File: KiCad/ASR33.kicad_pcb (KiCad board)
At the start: 2 copper layers, 45 x 38 mm, 42 parts, among them J1 USB-C, J2 DC, J3 Power, J4 RUN, J5 Tx, J6 Rx, Q1 NX7002AK, SW1 SW_Push, U1 ESP32-WROOM-32, U2 FT231XQ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

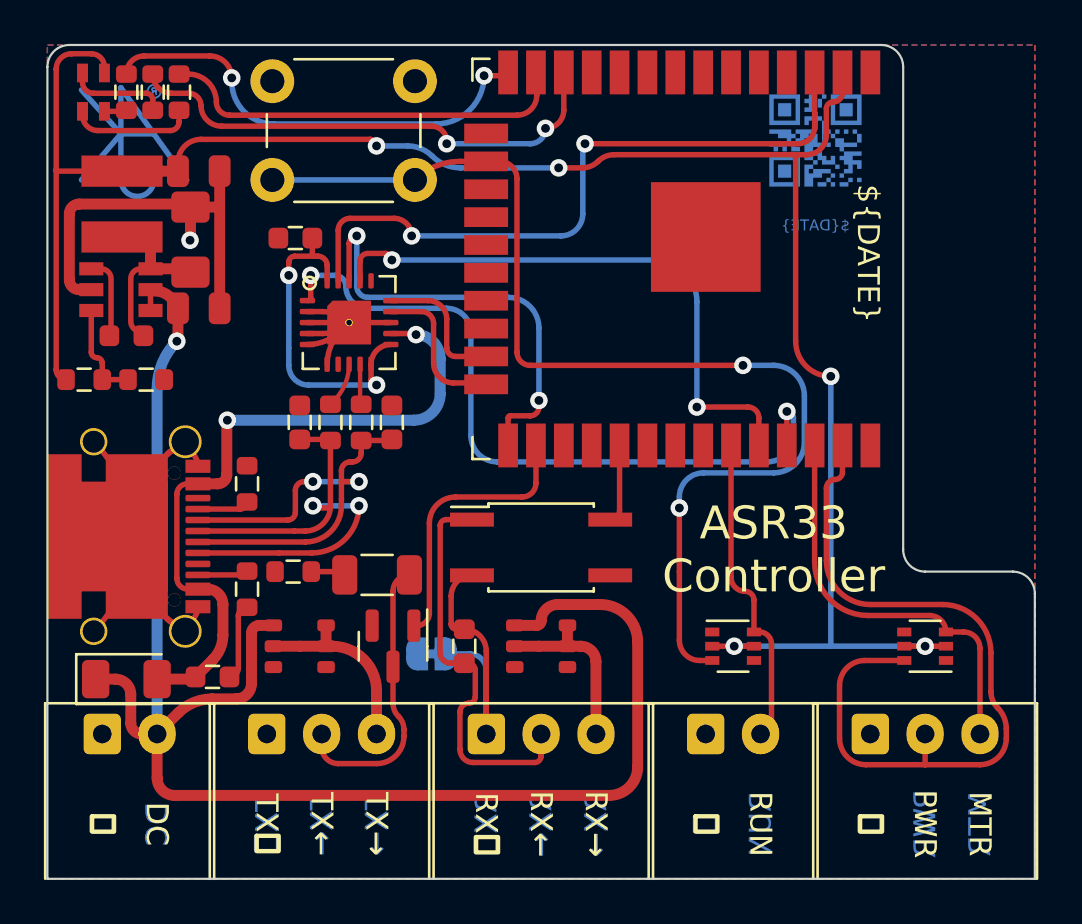
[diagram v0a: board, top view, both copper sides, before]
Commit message: Label GPIOs on silkscreen
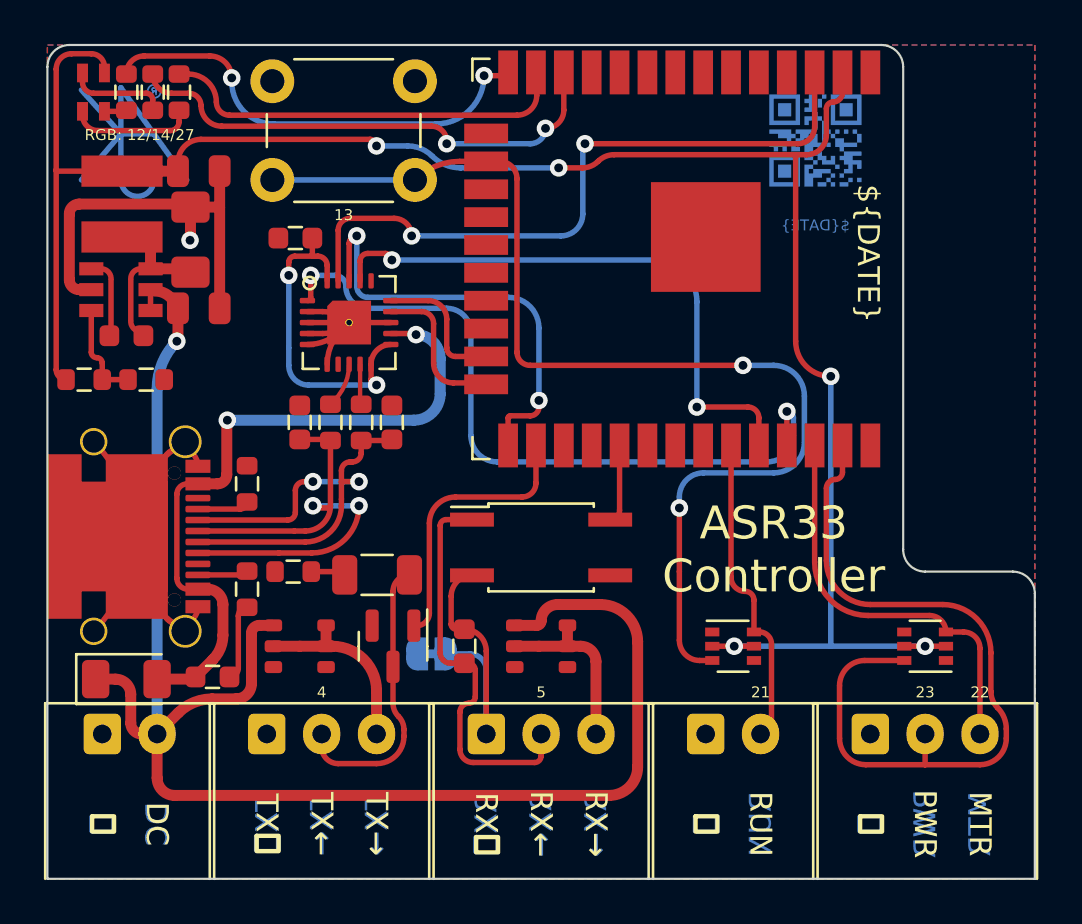
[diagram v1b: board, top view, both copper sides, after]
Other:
- board text added: "13"
- board text added: "21"
- board text added: "22"
- board text added: "23"
- board text added: "4"
- board text added: "5"
- board text added: "RGB: 12/14/27"
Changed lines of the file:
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@@
     )
   )
-  (property "DATE" "2022-01-29")
+  (property "DATE" "2022-01-30")
   (net 0 "")
   (net 1 "D+")
@@
     (effects (font (size 1 1) (thickness 0.2)))
   )
+  (gr_text "22" (at 162.5 111.5) (layer "F.SilkS")
+    (effects (font (size 0.5 0.5) (thickness 0.08)))
+  )
   (gr_text "⏚" (at 122.5 117.5 270) (layer "F.SilkS")
     (effects (font (size 1 1) (thickness 0.2)))
@@
     (effects (font (size 1 1) (thickness 0.2)))
   )
+  (gr_text "RGB: 12/14/27" (at 124.2 86.1) (layer "F.SilkS")
+    (effects (font (size 0.5 0.5) (thickness 0.08)))
+  )
   (gr_text "TX←" (at 132.5 117.5 270) (layer "F.SilkS")
     (effects (font (size 1 1) (thickness 0.2)))
@@
     (effects (font (size 1 1) (thickness 0.2)))
   )
+  (gr_text "21" (at 152.5 111.5) (layer "F.SilkS")
+    (effects (font (size 0.5 0.5) (thickness 0.08)))
+  )
   (gr_text "TX→" (at 135 117.5 270) (layer "F.SilkS")
     (effects (font (size 1 1) (thickness 0.2)))
   )
+  (gr_text "5" (at 142.5 111.5) (layer "F.SilkS")
+    (effects (font (size 0.5 0.5) (thickness 0.08)))
+  )
   (gr_text "⏚" (at 150 117.5 270) (layer "F.SilkS")
     (effects (font (size 1 1) (thickness 0.2)))
@@
     (effects (font (size 1 1) (thickness 0.2)))
   )
+  (gr_text "13" (at 133.5 89.75) (layer "F.SilkS")
+    (effects (font (size 0.5 0.5) (thickness 0.08)))
+  )
+  (gr_text "4" (at 132.5 111.5) (layer "F.SilkS")
+    (effects (font (size 0.5 0.5) (thickness 0.08)))
+  )
   (gr_text "RX⏚" (at 140 117.5 270) (layer "F.SilkS")
     (effects (font (size 1 1) (thickness 0.2)))
   )
+  (gr_text "23" (at 160 111.5) (layer "F.SilkS")
+    (effects (font (size 0.5 0.5) (thickness 0.08)))
+  )
   (gr_text "RX→" (at 145 117.5 270) (layer "F.SilkS")

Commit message: 60mA
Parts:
- removed the C5 at (135.0, 106.2)
- removed the C6 at (139.0, 109.4)
- removed R10: 470R NF, RevK:R_0603
- added JP2: 20R NF, RevK:Pad_1206_0805_Open, F.Cu at (141.8, 109.0)
- added JP3: GND-Linked, RevK:Pad_1206_0805_Bridged, B.Cu at (137.3, 109.8)
- added JP4: 20R NF, RevK:Pad_1206_0805_Open, F.Cu at (139.6, 104.6)
- JP1: value Rx-RTN -> 20R NF; footprint RevK:SolderJumper-2_P1.3mm_Bridged2Bar_RoundedPad1.0x1.5mm -> RevK:Pad_1206_0805_Open; moved to F.Cu
- U5: value LTV-355T -> LTV-356T
- moved JP1 6.54 mm to (131.0, 109.0), turned to 90 degrees
- moved Q1 5.89 mm to (136.8, 103.6)
- moved U3 2.50 mm to (134.0, 109.4)
- moved U5 2.42 mm to (144.9, 104.6)
- moved U4 2.25 mm to (144.8, 109.4)
- renumbered C7 to C5, C8 to C6, C9 to C7
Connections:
- J6 pad 1: Net-(C6-Pad1) -> Net-(J6-Pad1)
- JP1 pad 1: GND -> Net-(JP1-Pad1)
- JP1 pad 2: Net-(C6-Pad1) -> DC
- U3 pad 6: unconnected-(U3-Pad6) -> Net-(JP1-Pad1)
- U4 pad 6: unconnected-(U4-Pad6) -> Net-(JP2-Pad1)
- U5 pad 2: Net-(C6-Pad1) -> Net-(J6-Pad1)
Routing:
- net Net-(J6-Pad1): track 0.00 -> 15.5 mm
- net Net-(C6-Pad1): track 13.9 -> 0.00 mm
- net TX20MA: track 12.7 -> 6.17 mm
- net DC: track 71.8 -> 75.2 mm
- net Net-(JP2-Pad1): track 0.00 -> 1.86 mm
- net Net-(JP1-Pad1): track 0.00 -> 1.86 mm
- net Net-(C5-Pad2): track 1.60 -> 0.00 mm
- net BUTTON: track 51.5 -> 50.0 mm
- net Net-(J5-Pad2): track 13.3 -> 14.5 mm
- net Net-(J6-Pad3): track 8.32 -> 7.40 mm
- net Net-(J5-Pad3): track 8.70 -> 7.83 mm
- net RX20MA: track 3.61 -> 4.13 mm
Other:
- board text added: "20R"
- board text added: "Fit for 60mA"

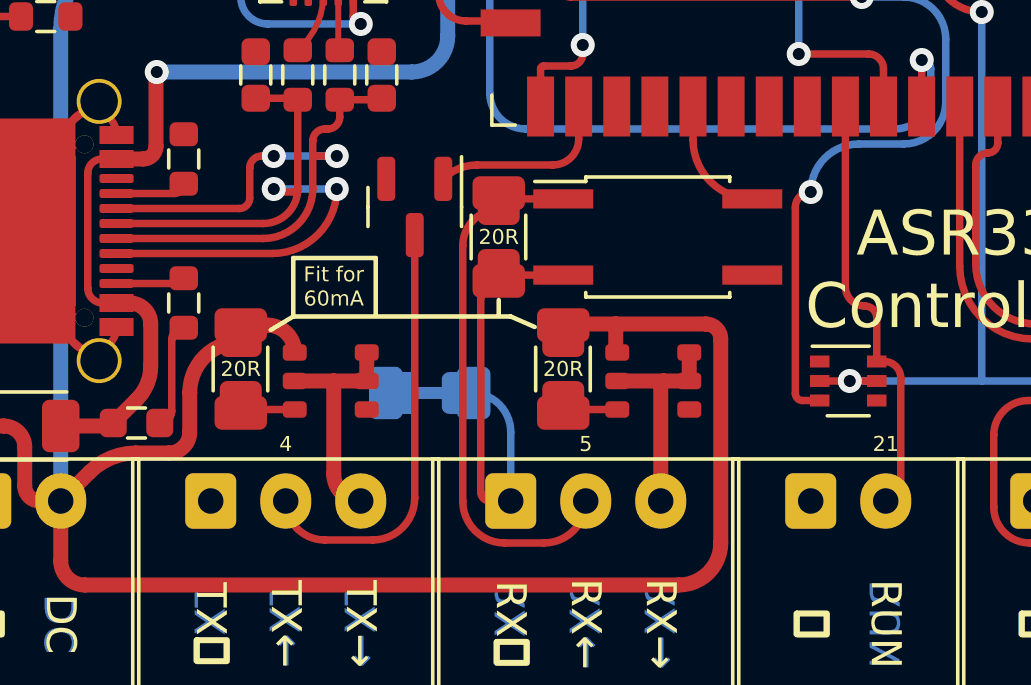
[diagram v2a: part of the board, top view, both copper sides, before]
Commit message: More on 60mA
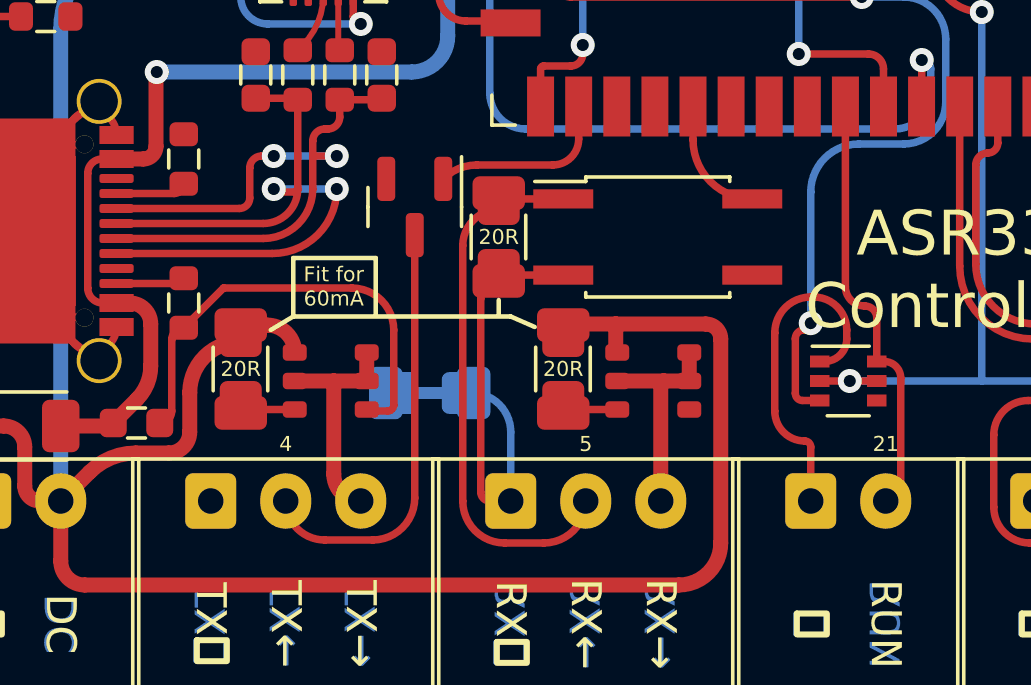
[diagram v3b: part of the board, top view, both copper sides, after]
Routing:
- net GND: track 16.9 -> 40.2 mm
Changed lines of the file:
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@@
   (gr_arc (start 123.25 104.25) (mid 123.78033 104.46967) (end 124 105) (layer "B.SilkS") (width 0.15))
   (gr_line (start 140 112.5) (end 139.96967 110.3) (layer "B.SilkS") (width 0.15))
-  (gr_arc (start 139.46967 109.78033) (mid 139.8261 109.937764) (end 139.96967 110.3) (layer "B.SilkS") (width 0.15))
+  (gr_arc (start 139.46967 109.78033) (mid 139.826099 109.937764) (end 139.96967 110.3) (layer "B.SilkS") (width 0.15))
   (gr_line (start 124 105) (end 124 110.5) (layer "B.SilkS") (width 0.15))
   (gr_line (start 130 112.4) (end 130 110.5) (layer "B.SilkS") (width 0.15))
@@
   (arc (start 133.75 96.55) (mid 133.570823 97.450782) (end 133.060571 98.214429) (width 0.2) (layer "F.Cu") (net 1))
   (segment (start 133.386396 95.013604) (end 133.75 94.65) (width 0.25) (layer "F.Cu") (net 2))
+  (segment (start 150 111.6) (end 150 113.4) (width 0.25) (layer "F.Cu") (net 2))
   (segment (start 131.85 94.65) (end 133.75 94.65) (width 0.25) (layer "F.Cu") (net 2))
+  (segment (start 151.2 108) (end 151.2 107.7) (width 0.25) (layer "F.Cu") (net 2))
   (segment (start 126.52 89.3875) (end 126.52 90.851716) (width 0.5) (layer "F.Cu") (net 2))
   (segment (start 135.65 94.65) (end 133.75 94.65) (width 0.25) (layer "F.Cu") (net 2))
   (segment (start 128.7 108.025) (end 128.7 110.4) (width 0.25) (layer "F.Cu") (net 2))
+  (segment (start 136.1 107.7) (end 136.1 110.2) (width 0.25) (layer "F.Cu") (net 2))
   (segment (start 131.85 94.15) (end 132.542894 94.15) (width 0.25) (layer "F.Cu") (net 2))
+  (segment (start 135.9 110.4) (end 135.25 110.4) (width 0.25) (layer "F.Cu") (net 2))
+  (segment (start 150.3 108.75) (end 150.45 108.75) (width 0.25) (layer "F.Cu") (net 2))
+  (segment (start 130.425 106.3) (end 134.7 106.3) (width 0.25) (layer "F.Cu") (net 2))
+  (segment (start 150.1 106.6) (end 150 106.6) (width 0.25) (layer "F.Cu") (net 2))
+  (segment (start 129.1 107.625) (end 130.425 106.3) (width 0.25) (layer "F.Cu") (net 2))
+  (segment (start 148.8 107.8) (end 148.8 110.4) (width 0.25) (layer "F.Cu") (net 2))
   (segment (start 131.85 95.15) (end 132.542894 95.15) (width 0.25) (layer "F.Cu") (net 2))
   (via (at 126.5 90.9) (size 0.8) (drill 0.4) (layers "F.Cu" "B.Cu") (net 2))
+  (arc (start 150 106.6) (mid 149.151472 106.951472) (end 148.8 107.8) (width 0.25) (layer "F.Cu") (net 2))
   (arc (start 132.542894 95.15) (mid 133.196175 95.020054) (end 133.75 94.65) (width 0.25) (layer "F.Cu") (net 2))
+  (arc (start 148.8 110.4) (mid 149.092893 111.107107) (end 149.8 111.4) (width 0.25) (layer "F.Cu") (net 2))
   (arc (start 128.7 110.4) (mid 128.582843 110.682843) (end 128.3 110.8) (width 0.25) (layer "F.Cu") (net 2))
+  (arc (start 149.8 111.4) (mid 149.941421 111.458579) (end 150 111.6) (width 0.25) (layer "F.Cu") (net 2))
+  (arc (start 134.7 106.3) (mid 135.689949 106.710051) (end 136.1 107.7) (width 0.25) (layer "F.Cu") (net 2))
+  (arc (start 150.45 108.75) (mid 150.98033 108.53033) (end 151.2 108) (width 0.25) (layer "F.Cu") (net 2))
   (arc (start 126.52 90.851716) (mid 126.514802 90.877847) (end 126.5 90.9) (width 0.5) (layer "F.Cu") (net 2))
+  (arc (start 136.1 110.2) (mid 136.041421 110.341421) (end 135.9 110.4) (width 0.25) (layer "F.Cu") (net 2))
   (arc (start 133.386397 95.013603) (mid 132.915395 95.718508) (end 132.75 96.55) (width 0.25) (layer "F.Cu") (net 2))
+  (arc (start 151.2 107.7) (mid 150.877817 106.922183) (end 150.1 106.6) (width 0.25) (layer "F.Cu") (net 2))
   (arc (start 132.542894 94.15) (mid 133.196175 94.279946) (end 133.75 94.65) (width 0.25) (layer "F.Cu") (net 2))
   (arc (start 131.85 95.65) (mid 132.681492 95.484606) (end 133.386396 95.013604) (width 0.25) (layer "F.Cu") (net 2))
+  (arc (start 135.25 110.4) (mid 135.214645 110.385355) (end 135.2 110.35) (width 0.25) (layer "F.Cu") (net 2))
   (arc (start 129.1 107.625) (mid 128.817157 107.742157) (end 128.7 108.025) (width 0.25) (layer "F.Cu") (net 2))
   (segment (start 134.25 96.55) (end 134.25 98.25429) (width 0.2) (layer "F.Cu") (net 3))
@@
   (segment (start 143.55 110.35) (end 141.8625 110.35) (width 0.25) (layer "F.Cu") (net 46))
   (arc (start 141.8625 110.35) (mid 141.78295 110.38295) (end 141.75 110.4625) (width 0.25) (layer "F.Cu") (net 46))
-  (segment (start 149.485932 103.614068) (end 149.485932 109.810932) (width 0.25) (layer "F.Cu") (net 51))
+  (segment (start 149.485932 107.985932) (end 149.485932 109.810932) (width 0.25) (layer "F.Cu") (net 51))
   (segment (start 140.605 87.305) (end 139.995 87.305) (width 0.25) (layer "F.Cu") (net 51))
   (segment (start 138.79001 87.305) (end 139.995 87.305) (width 0.25) (layer "F.Cu") (net 51))
@@
   (segment (start 151.7 96.6) (end 142 96.6) (width 0.25) (layer "F.Cu") (net 51))
   (via (at 151.7 96.6) (size 0.8) (drill 0.4) (layers "F.Cu" "B.Cu") (net 51))
-  (via (at 150 103.1) (size 0.8) (drill 0.4) (layers "F.Cu" "B.Cu") (net 51))
+  (via (at 150 107.471864) (size 0.8) (drill 0.4) (layers "F.Cu" "B.Cu") (net 51))
+  (arc (start 149.771864 107.7) (mid 149.56968 107.783748) (end 149.485932 107.985932) (width 0.25) (layer "F.Cu") (net 51))
   (arc (start 149.485932 109.810932) (mid 149.555953 109.979979) (end 149.725 110.05) (width 0.25) (layer "F.Cu") (net 51))
-  (arc (start 150 103.1) (mid 149.636499 103.250567) (end 149.485932 103.614068) (width 0.25) (layer "F.Cu") (net 51))
   (arc (start 142 96.6) (mid 141.575736 96.424264) (end 141.4 96) (width 0.25) (layer "F.Cu") (net 51))
   (arc (start 136.75 88.15) (mid 137.685964 87.524609) (end 138.79001 87.305) (width 0.25) (layer "F.Cu") (net 51))
+  (arc (start 150 107.471864) (mid 149.933181 107.633181) (end 149.771864 107.7) (width 0.25) (layer "F.Cu") (net 51))
   (arc (start 141.4 88.1) (mid 141.16715 87.53785) (end 140.605 87.305) (width 0.25) (layer "F.Cu") (net 51))
   (segment (start 151.6 101.5) (end 153.1 101.5) (width 0.25) (layer "B.Cu") (net 51))
+  (segment (start 150 103.1) (end 150 107.471864) (width 0.25) (layer "B.Cu") (net 51))
   (segment (start 154.5 100.1) (end 154.5 98) (width 0.25) (layer "B.Cu") (net 51))
   (segment (start 136.75 88.15) (end 130.25 88.15) (width 0.25) (layer "B.Cu") (net 51))
